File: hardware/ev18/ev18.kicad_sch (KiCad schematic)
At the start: 226 parts, among them CN1 Conn_05x02_Female, CN2 PJ-242, J1 USB_C_Receptacle, J10 Conn_02x05_Counter_Clockwise, J11 Conn_02x05_Counter_Clockwise, J12 Conn_01x01, J13 Conn_01x01, J14 Conn_01x01, J15 Conn_01x01, J16 Conn_01x01, J17 Conn_01x01, J18 Conn_01x01, J19 Conn_01x01, J2 Conn_01x02_Socket, J20 Conn_02x05_Counter_Clockwise, J21 Conn_01x01, J22 USB_C_Receptacle, J23 Conn_01x01, J3 AudioJack4, J4 Conn_02x03_Odd_Even, J5 Conn_02x03_Odd_Even, J6 Conn_02x05_Counter_Clockwise, J7 Conn_02x05_Counter_Clockwise, J8 Conn_02x05_Counter_Clockwise, J9 Conn_02x05_Counter_Clockwise, Q1 2N7002, Q2 2N7002, Q3 2N7002, SW1 SW_SPDT, SW2 SW_Push, SW3 SW_Push, SW4 SW_Push, SW5 SW_Push, SW6 SW_Push, SW7 SW_Push, SW8 SW_Push, U1 BQ21040DBV, U10 STM32F405RGTx, U11 USBLC6-2P6, U12 XC6227C301MR-G, U2 USBLC6-2P6, U3 STM32F072CBTx, U4 CH340C, U5 TPS63060, U6 WM8960CGEFL/RV, U7 ESP32-S3-WROOM-1, U8 M24C02-RMN6TP, U9 TPS2116DRL, Y1 Crystal_GND24

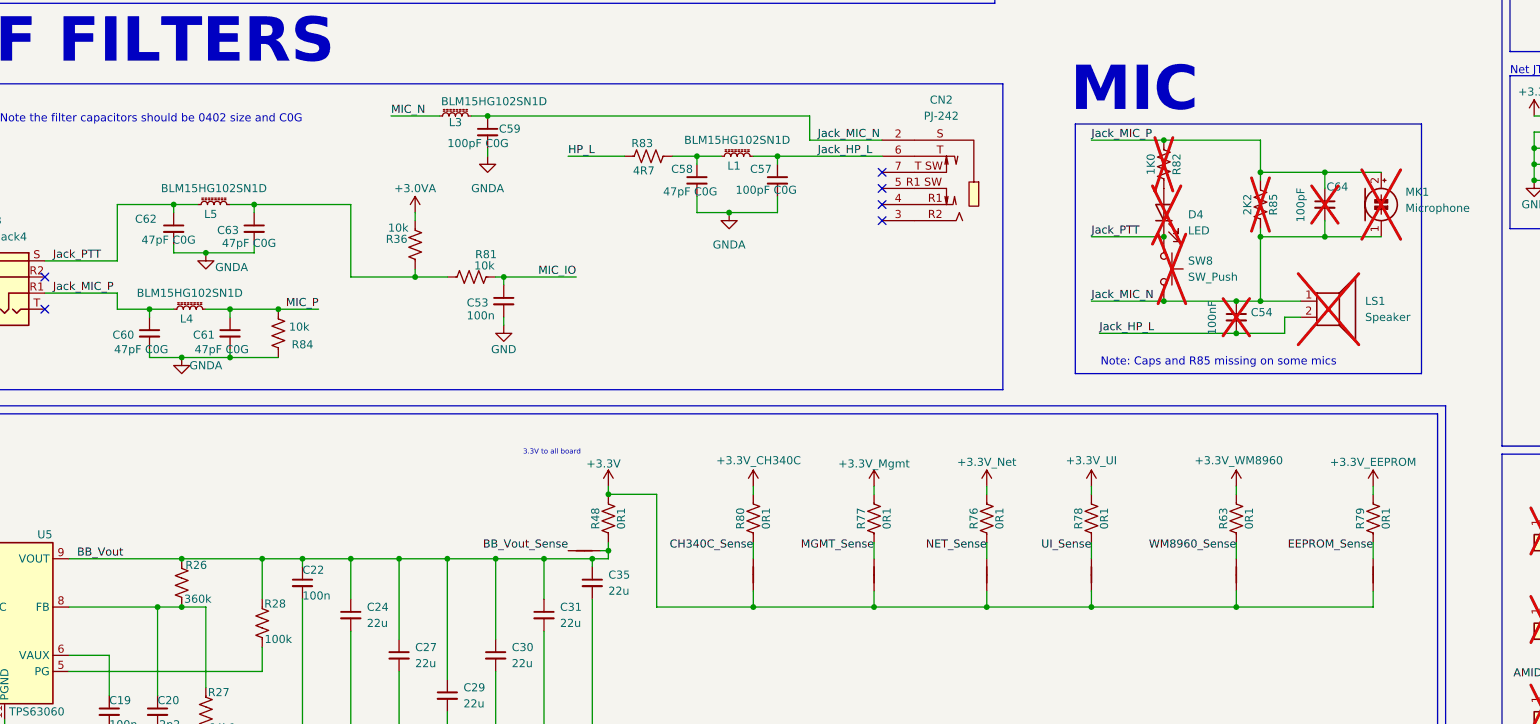
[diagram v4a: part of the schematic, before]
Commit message: Added jlcpcb part numbers to the capacitors, to R83, and the ferrite beads
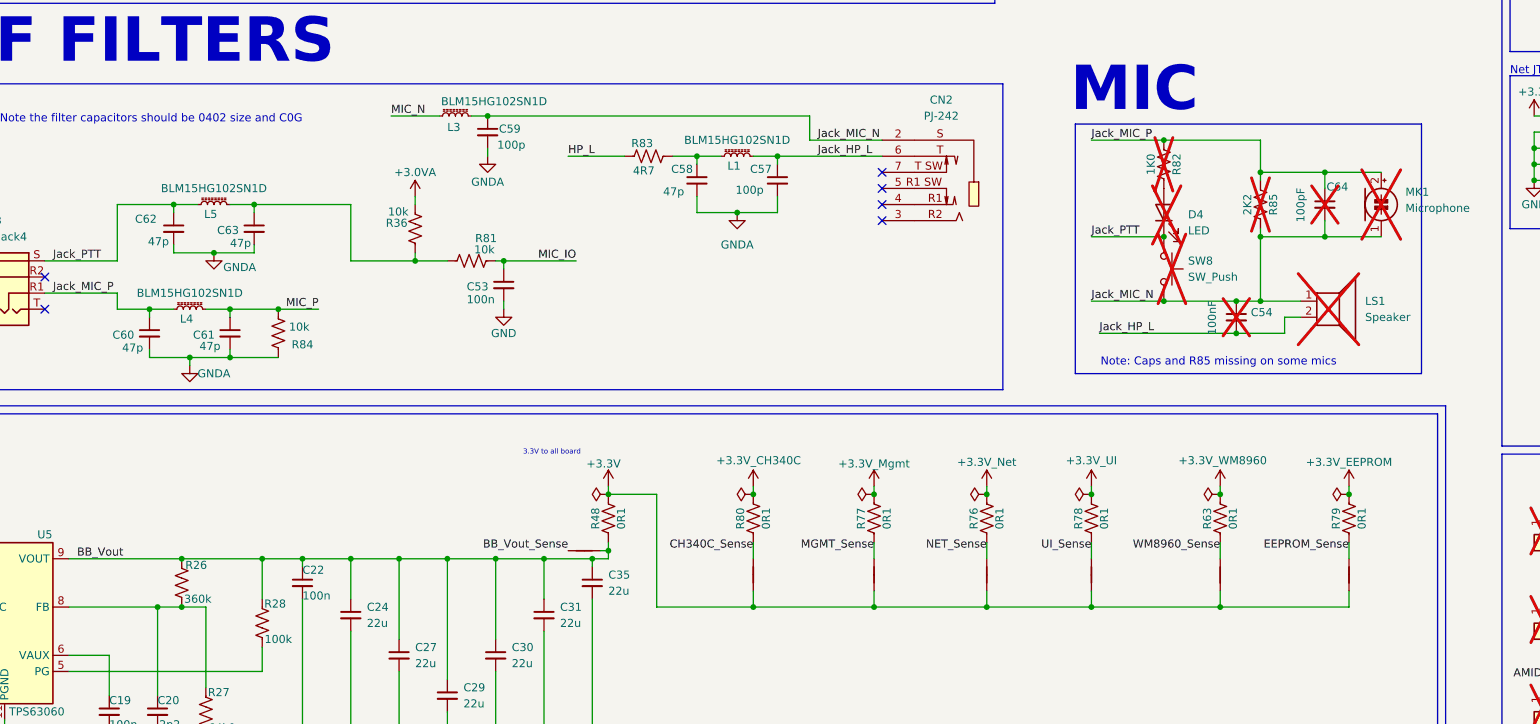
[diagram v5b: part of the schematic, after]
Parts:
- C57: value 100pF C0G -> 100p; JLCPCB Part # (none) -> C1546
- C58, C60, C61, C62, C63: value 47pF C0G -> 47p; JLCPCB Part # (none) -> C1567
- C59: value 100pF C0G -> 100p; JLCPCB Part # (none) -> V
- L1, L3, L4, L5: JLCPCB Part # (none) -> C76889
- R83: JLCPCB Part # (none) -> C25792
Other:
- moved on the sheet: C53, R36, R63, R79, R81

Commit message: Changed R83's part number to be a 4R7 instead of 47K. Changed the footprint to match
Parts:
- R83: footprint Resistor_SMD:R_0402_1005Metric -> Resistor_SMD:R_0603_1608Metric; JLCPCB Part # C25792 -> C23164
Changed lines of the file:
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@@
 			)
 		)
-		(property "Footprint" "Resistor_SMD:R_0402_1005Metric"
+		(property "Footprint" "Resistor_SMD:R_0603_1608Metric"
 			(at 320.04 260.858 90)
 			(effects
@@
 			)
 		)
-		(property "JLCPCB Part #" "C25792"
+		(property "JLCPCB Part #" "C23164"
 			(at 320.04 259.08 0)
 			(effects

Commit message: Fixed error with part number in C59
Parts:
- C59: JLCPCB Part # V -> C1546
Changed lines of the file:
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@@
 			)
 		)
-		(property "JLCPCB Part #" "V"
+		(property "JLCPCB Part #" "C1546"
 			(at 294.64 255.27 0)
 			(effects
